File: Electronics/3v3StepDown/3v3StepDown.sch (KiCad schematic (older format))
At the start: 5 parts

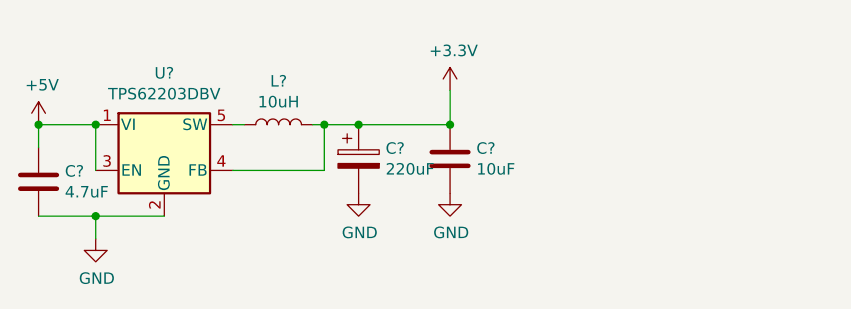
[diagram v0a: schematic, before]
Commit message: 3v3StepDown module
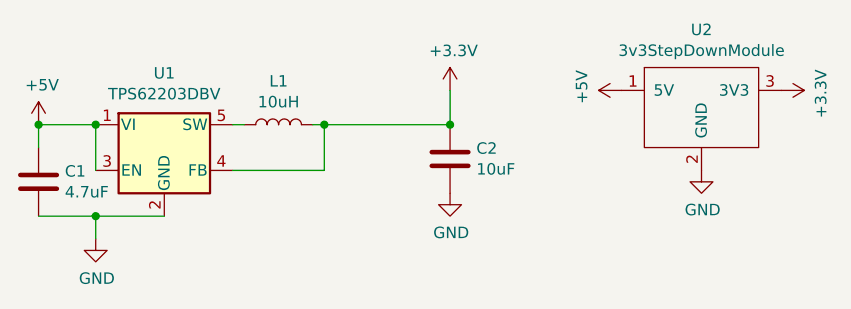
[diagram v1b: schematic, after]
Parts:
- removed C?: 220uF, Capacitor_SMD:CP_Elec_8x10.5, symbol EggbotWireless-rescue:CP-Device
- added U2: 3v3StepDownModule, Connector_PinHeader_2.54mm:PinHeader_1x03_P2.54mm_Horizontal, symbol 3v3StepDown:3v3StepDownModule
- C1, C2: renamed from C?; footprint Capacitor_SMD:C_0805_2012Metric_Pad1.15x1.40mm_HandSolder -> Capacitor_SMD:C_0805_2012Metric_Pad1.18x1.45mm_HandSolder
- gave numbers to parts that had none: 2
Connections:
- net +3V3: now also U2.3 (3V3)
- net +5V: now also U2.1 (5V)
- net GND: now also U2.2 (GND)
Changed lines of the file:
@@
 $EndDescr
 $Comp
-L EggbotWireless-rescue:L-Device L?
+L EggbotWireless-rescue:L-Device L1
 U 1 1 5FECC753
 P 5200 3200
-F 0 "L?" V 5390 3200 50  0000 C CNN
+F 0 "L1" V 5390 3200 50  0000 C CNN
 F 1 "10uH" V 5299 3200 50  0000 C CNN
 F 2 "Inductor_SMD:L_6.3x6.3_H3" H 5200 3200 50  0001 C CNN
@@
 $EndComp
 $Comp
-L EggbotWireless-rescue:C-Device C?
+L EggbotWireless-rescue:C-Device C2
 U 1 1 5FECC759
 P 5950 3350
-F 0 "C?" H 6065 3396 50  0000 L CNN
+F 0 "C2" H 6065 3396 50  0000 L CNN
 F 1 "10uF" H 6065 3305 50  0000 L CNN
-F 2 "Capacitor_SMD:C_0805_2012Metric_Pad1.15x1.40mm_HandSolder" H 5988 3200 50  0001 C CNN
+F 2 "Capacitor_SMD:C_0805_2012Metric_Pad1.18x1.45mm_HandSolder" H 5988 3200 50  0001 C CNN
 F 3 "~" H 5950 3350 50  0001 C CNN
 	1    5950 3350
@@
 $EndComp
 $Comp
-L EggbotWireless-rescue:C-Device C?
+L EggbotWireless-rescue:C-Device C1
 U 1 1 5FECC75F
 P 4150 3450
-F 0 "C?" H 4265 3496 50  0000 L CNN
+F 0 "C1" H 4265 3496 50  0000 L CNN
 F 1 "4.7uF" H 4265 3405 50  0000 L CNN
-F 2 "Capacitor_SMD:C_0805_2012Metric_Pad1.15x1.40mm_HandSolder" H 4188 3300 50  0001 C CNN
+F 2 "Capacitor_SMD:C_0805_2012Metric_Pad1.18x1.45mm_HandSolder" H 4188 3300 50  0001 C CNN
 F 3 "~" H 4150 3450 50  0001 C CNN
 	1    4150 3450
@@
 	4400 3200 4150 3200
 $Comp
-L EggbotWireless-rescue:GND-power-Catfi-rescue #PWR?
+L EggbotWireless-rescue:GND-power-Catfi-rescue #PWR0101
 U 1 1 5FECC767
 P 4400 3700
-F 0 "#PWR?" H 4400 3450 50  0001 C CNN
+F 0 "#PWR0101" H 4400 3450 50  0001 C CNN
 F 1 "GND" H 4405 3527 50  0000 C CNN
 F 2 "" H 4400 3700 50  0001 C CNN
@@
 	4400 3600 4700 3600
 $Comp
-L EggbotWireless-rescue:TPS62203DBV-Regulator_Switching U?
+L EggbotWireless-rescue:TPS62203DBV-Regulator_Switching U1
 U 1 1 5FECC771
 P 4700 3400
-F 0 "U?" H 4700 3825 50  0000 C CNN
+F 0 "U1" H 4700 3825 50  0000 C CNN
 F 1 "TPS62203DBV" H 4700 3734 50  0000 C CNN
 F 2 "Package_TO_SOT_SMD:SOT-23-5" H 4750 3250 50  0001 L CIN
@@
 Connection ~ 5400 3200
 $Comp
-L EggbotWireless-rescue:GND-power-Catfi-rescue #PWR?
+L EggbotWireless-rescue:GND-power-Catfi-rescue #PWR0102
 U 1 1 5FECC77C
 P 5950 3500
-F 0 "#PWR?" H 5950 3250 50  0001 C CNN
+F 0 "#PWR0102" H 5950 3250 50  0001 C CNN
 F 1 "GND" H 5955 3327 50  0000 C CNN
 F 2 "" H 5950 3500 50  0001 C CNN
@@
 	5000 3400 5400 3400
 $Comp
-L EggbotWireless-rescue:+5V-power #PWR?
+L EggbotWireless-rescue:+5V-power #PWR0103
 U 1 1 5FECC786
 P 4150 3200
-F 0 "#PWR?" H 4150 3050 50  0001 C CNN
+F 0 "#PWR0103" H 4150 3050 50  0001 C CNN
 F 1 "+5V" H 4165 3373 50  0000 C CNN
 F 2 "" H 4150 3200 50  0001 C CNN
@@
 Connection ~ 4150 3200
 $Comp
-L EggbotWireless-rescue:+3.3V-power #PWR?
+L EggbotWireless-rescue:+3.3V-power #PWR0104
 U 1 1 5FECC78D
 P 5950 3050
-F 0 "#PWR?" H 5950 2900 50  0001 C CNN
+F 0 "#PWR0104" H 5950 2900 50  0001 C CNN
 F 1 "+3.3V" H 5965 3223 50  0000 C CNN
 F 2 "" H 5950 3050 50  0001 C CNN
@@
 $EndComp
 $Comp
-L EggbotWireless-rescue:CP-Device C?
-U 1 1 5FECC793
-P 5550 3350
-F 0 "C?" H 5668 3396 50  0000 L CNN
-F 1 "220uF" H 5668 3305 50  0000 L CNN
-F 2 "Capacitor_SMD:CP_Elec_8x10.5" H 5588 3200 50  0001 C CNN
-F 3 "~" H 5550 3350 50  0001 C CNN
-	1    5550 3350
+L 3v3StepDown:3v3StepDownModule U2
+U 1 1 5FCE3678
+P 7050 3050
+F 0 "U2" H 7050 3315 50  0000 C CNN
+F 1 "3v3StepDownModule" H 7050 3224 50  0000 C CNN
+F 2 "Connector_PinHeader_2.54mm:PinHeader_1x03_P2.54mm_Horizontal" H 7050 3050 50  0001 C CNN
+F 3 "" H 7050 3050 50  0001 C CNN
+	1    7050 3050
+	1    0    0    -1
+$EndComp
+$Comp
+L EggbotWireless-rescue:+5V-power #PWR0105
+U 1 1 5FCE3B7D
+P 6700 3050
+F 0 "#PWR0105" H 6700 2900 50  0001 C CNN
+F 1 "+5V" H 6715 3223 50  0000 C CNN
+F 2 "" H 6700 3050 50  0001 C CNN
+F 3 "" H 6700 3050 50  0001 C CNN
+	1    6700 3050
+	0    -1   -1   0
+$EndComp
+$Comp
+L EggbotWireless-rescue:+3.3V-power #PWR0106
+U 1 1 5FCE48F1
+P 7400 3050
+F 0 "#PWR0106" H 7400 2900 50  0001 C CNN
+F 1 "+3.3V" H 7415 3223 50  0000 C CNN
+F 2 "" H 7400 3050 50  0001 C CNN
+F 3 "" H 7400 3050 50  0001 C CNN
+	1    7400 3050
+	0    1    1    0
+$EndComp
+$Comp
+L EggbotWireless-rescue:GND-power-Catfi-rescue #PWR0107
+U 1 1 5FCE5458
+P 7050 3400
+F 0 "#PWR0107" H 7050 3150 50  0001 C CNN
+F 1 "GND" H 7055 3227 50  0000 C CNN
+F 2 "" H 7050 3400 50  0001 C CNN
+F 3 "" H 7050 3400 50  0001 C CNN
+	1    7050 3400
 	1    0    0    -1
 $EndComp
 Wire Wire Line
-	5550 3200 5950 3200
-Wire Wire Line
-	5400 3200 5550 3200
-Connection ~ 5550 3200
-$Comp
-L EggbotWireless-rescue:GND-power-Catfi-rescue #PWR?
-U 1 1 5FECC79C
-P 5550 3500
-F 0 "#PWR?" H 5550 3250 50  0001 C CNN
-F 1 "GND" H 5555 3327 50  0000 C CNN
-F 2 "" H 5550 3500 50  0001 C CNN
-F 3 "" H 5550 3500 50  0001 C CNN
-	1    5550 3500
-	1    0    0    -1
-$EndComp
+	5400 3200 5950 3200
 $EndSCHEMATC

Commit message: 3v3 boost in dip body
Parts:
- U2: footprint Connector_PinHeader_2.54mm:PinHeader_1x03_P2.54mm_Horizontal -> Package_DIP:DIP-4_W10.16mm
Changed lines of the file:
@@
 F 0 "U2" H 7050 3315 50  0000 C CNN
 F 1 "3v3StepDownModule" H 7050 3224 50  0000 C CNN
-F 2 "Connector_PinHeader_2.54mm:PinHeader_1x03_P2.54mm_Horizontal" H 7050 3050 50  0001 C CNN
+F 2 "Package_DIP:DIP-4_W10.16mm" H 7050 3050 50  0001 C CNN
 F 3 "" H 7050 3050 50  0001 C CNN
 	1    7050 3050
